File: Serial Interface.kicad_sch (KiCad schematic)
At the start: 34 parts, among them J23 *, J24 *, J25 *, J26 *, J27 *, J28 *, J29 *, J30 *, J31 *, J32 *, U7 *, U8 *

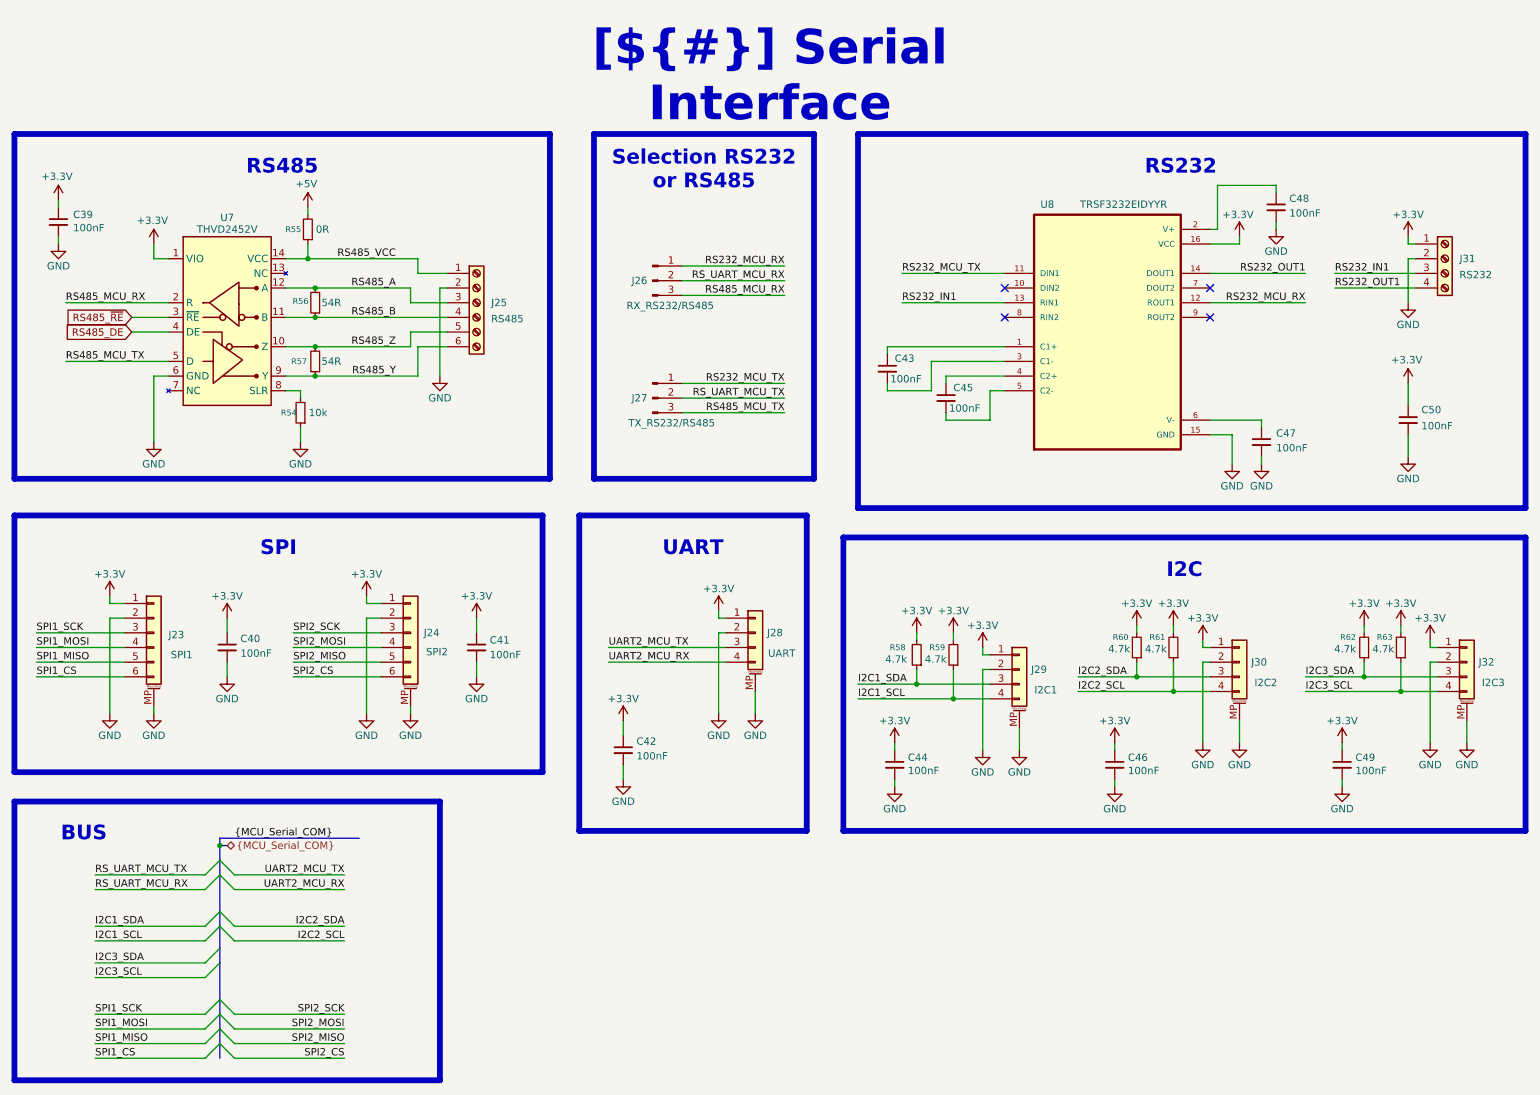
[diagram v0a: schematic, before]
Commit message: [Schematic][Modify] Annotation of all  the components
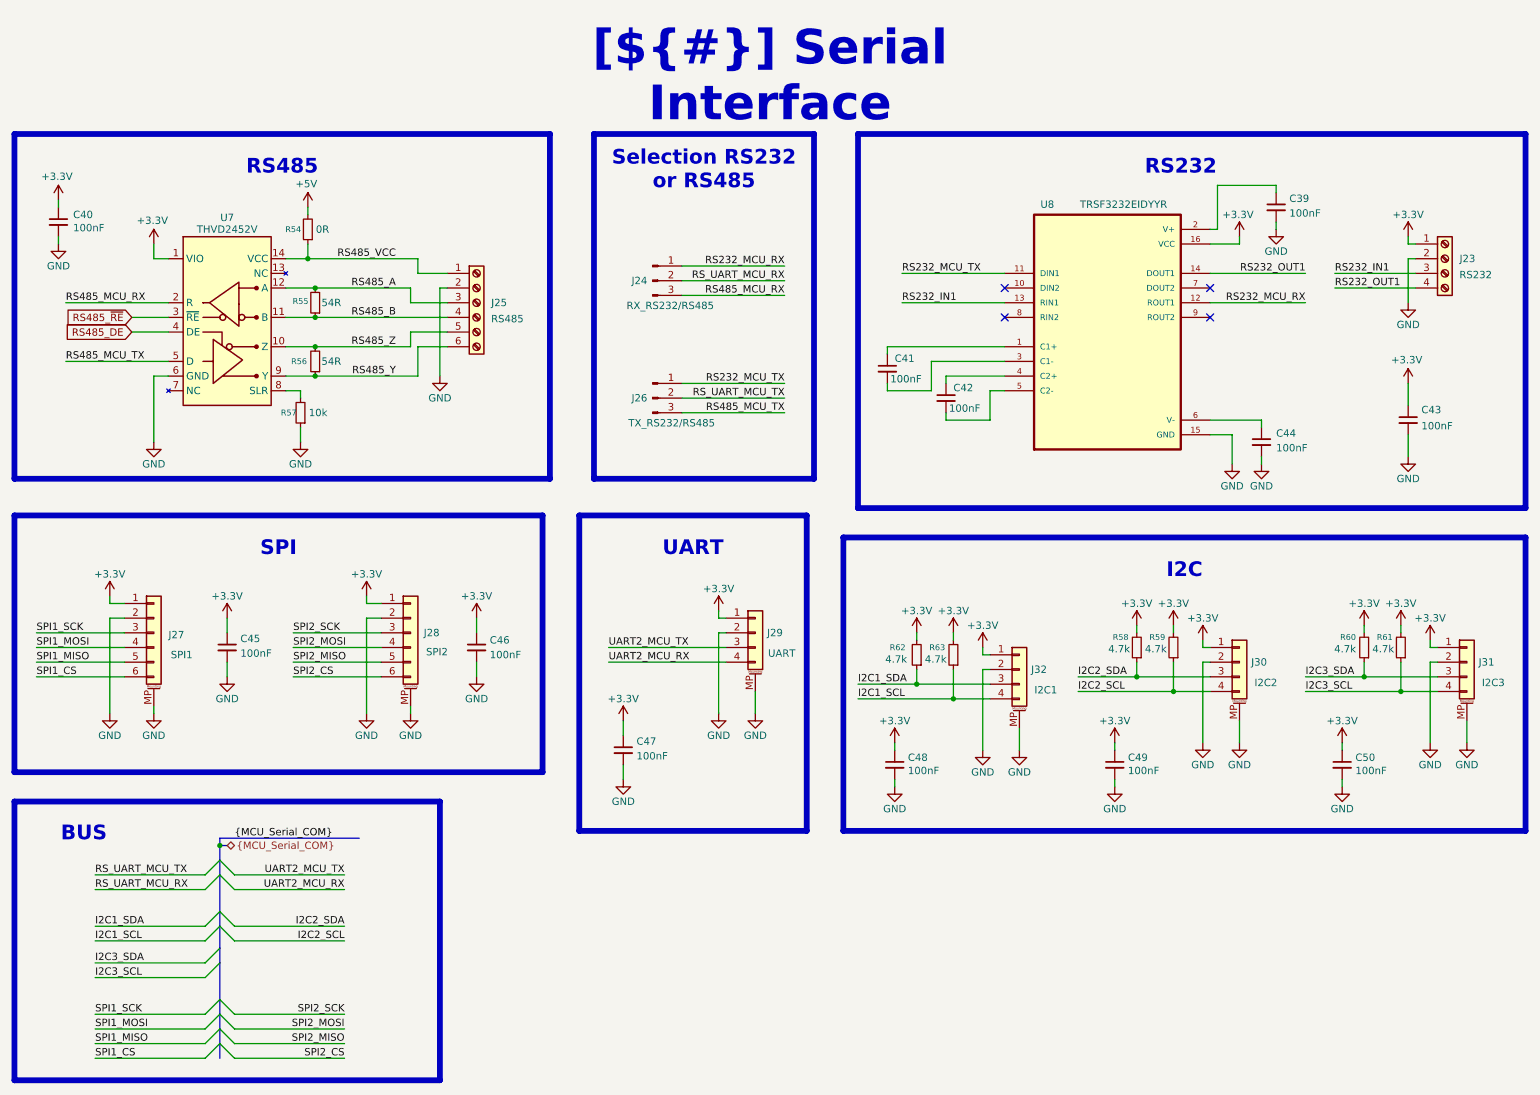
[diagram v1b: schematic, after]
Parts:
- renumbered C48 to C39, C39 to C40, C43 to C41, C45 to C42, C50 to C43, C47 to C44, C40 to C45, C41 to C46, C42 to C47, C44 to C48, C46 to C49, C49 to C50, J31 to J23, J26 to J24, J27 to J26, J23 to J27, J24 to J28, J28 to J29, J32 to J31, J29 to J32, R55 to R54, R56 to R55, R57 to R56, R54 to R57, R60 to R58, R61 to R59, R62 to R60, R63 to R61, R58 to R62, R59 to R63

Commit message: [Schematic][Modify] Monification of simulation models
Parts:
- C49: value 100nF -> 100n
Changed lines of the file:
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@@
 			)
 		)
-		(property "Value" "100nF"
+		(property "Value" "100n"
 			(at 210.566 141.986 0)
 			(effects
@@
 			)
 		)
+		(property "Sim.Device" "C"
+			(at 208.28 140.97 0)
+			(effects
+				(font
+					(size 1.27 1.27)
+				)
+			)
+		)
+		(property "Sim.Pins" "1=+ 2=-"
+			(at 208.28 140.97 0)
+			(effects
+				(font
+					(size 1.27 1.27)
+				)
+			)
+		)
 		(pin "2"
 		)
@@
 			)
 		)
+		(property "Sim.Library" ".\\"
+			(at 54.61 66.04 0)
+			(effects
+				(font
+					(size 1.27 1.27)
+				)
+				(hide yes)
+			)
+		)
 		(pin "5"
 		)
@@
 			(at 207.01 66.04 0)
 			(effects
+				(font
+					(size 1.27 1.27)
+				)
+				(hide yes)
+			)
+		)
+		(property "Sim.Library" ".\\"
+			(at 207.01 66.04 0)
+			(effects
